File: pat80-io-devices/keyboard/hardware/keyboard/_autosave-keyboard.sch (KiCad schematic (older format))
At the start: 117 parts, among them J3 Keyboard connector, SW1 1, SW10 3, SW11 E, SW12 D, SW13 C, SW14 V, SW15 F, SW16 R, SW17 4, SW18 5, SW19 T, SW2 Q, SW20 G, SW21 B, SW22 N, SW23 H, SW24 Y, SW25 6, SW26 7, SW27 U, SW28 J, SW29 M, SW3 A, SW30 ', SW31 K, SW32 I, SW33 8, SW34 9, SW35 O, SW36 L, SW37 P, SW38 [, SW39 ], SW4 Z, SW40 0, SW41 BACKSPACE, SW42 TILDE, SW43 TAB, SW44 ,, SW45 ., SW46 SPACE, SW47 /, SW48 ;, SW49 LSHIFT, SW5 X, SW50 CTRL, SW51 RSHIFT, SW52 RETURN, SW53 PATO, SW54 CAPSLK, SW6 S, SW7 W, SW8 2, SW9 CAPSLK_LED

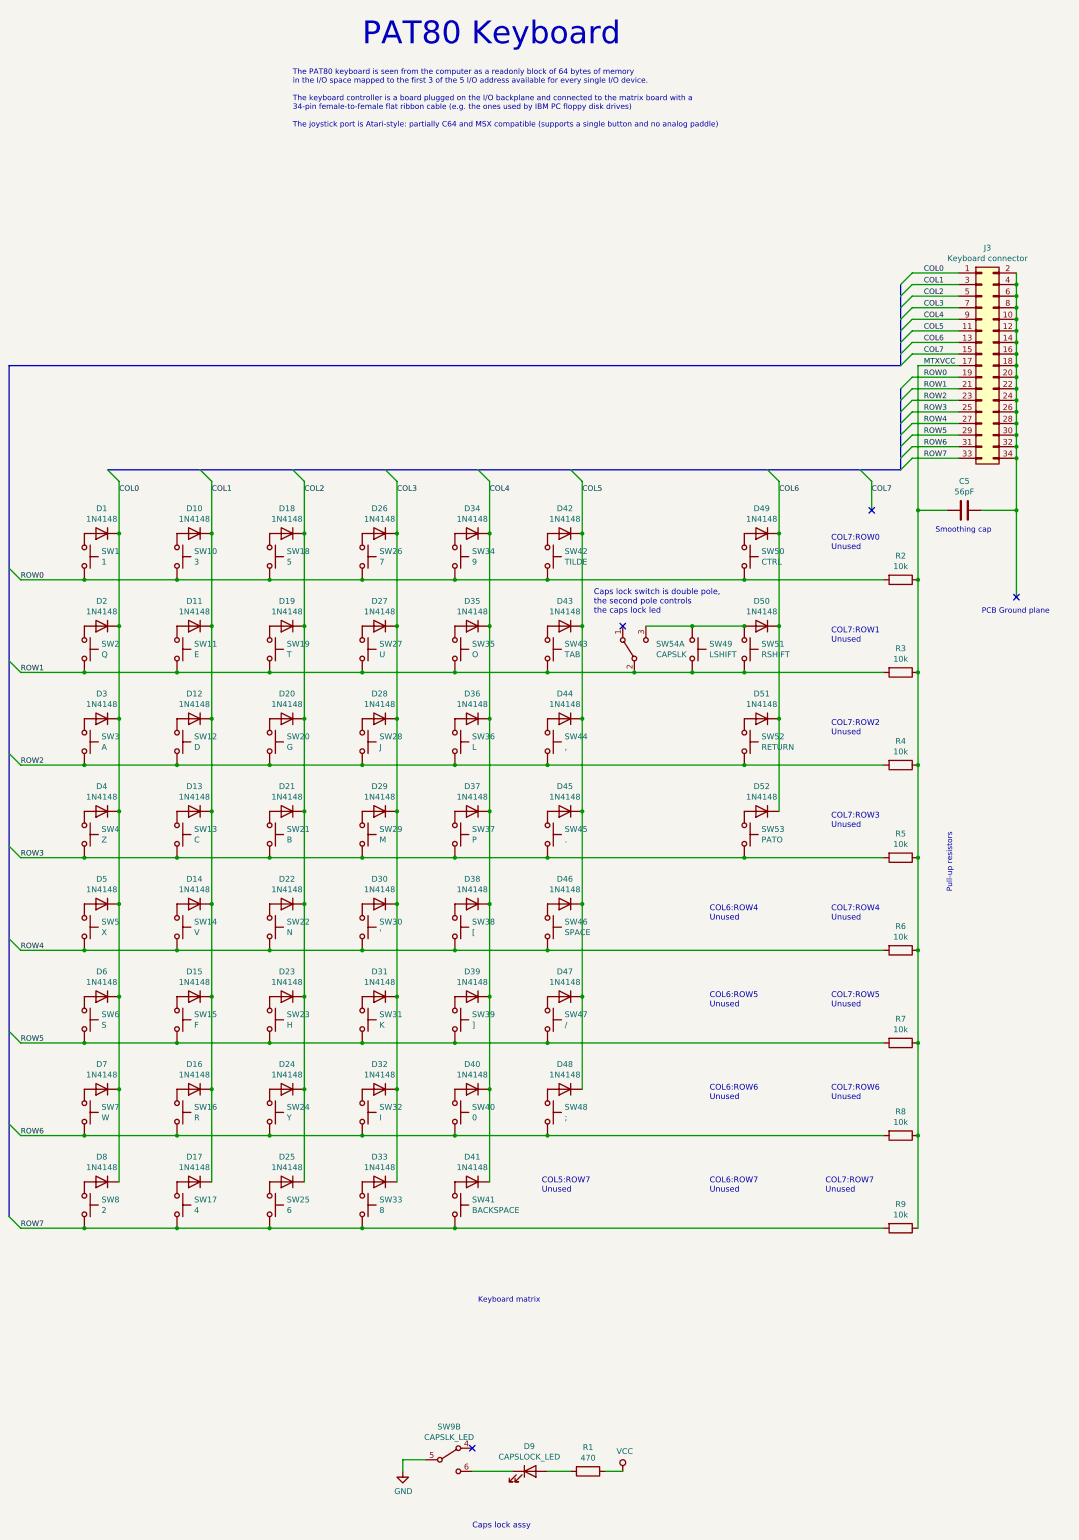
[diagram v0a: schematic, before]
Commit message: Split keyboard into two different schematics: kb controller and kb assembly. Started routing keyboard pcb.
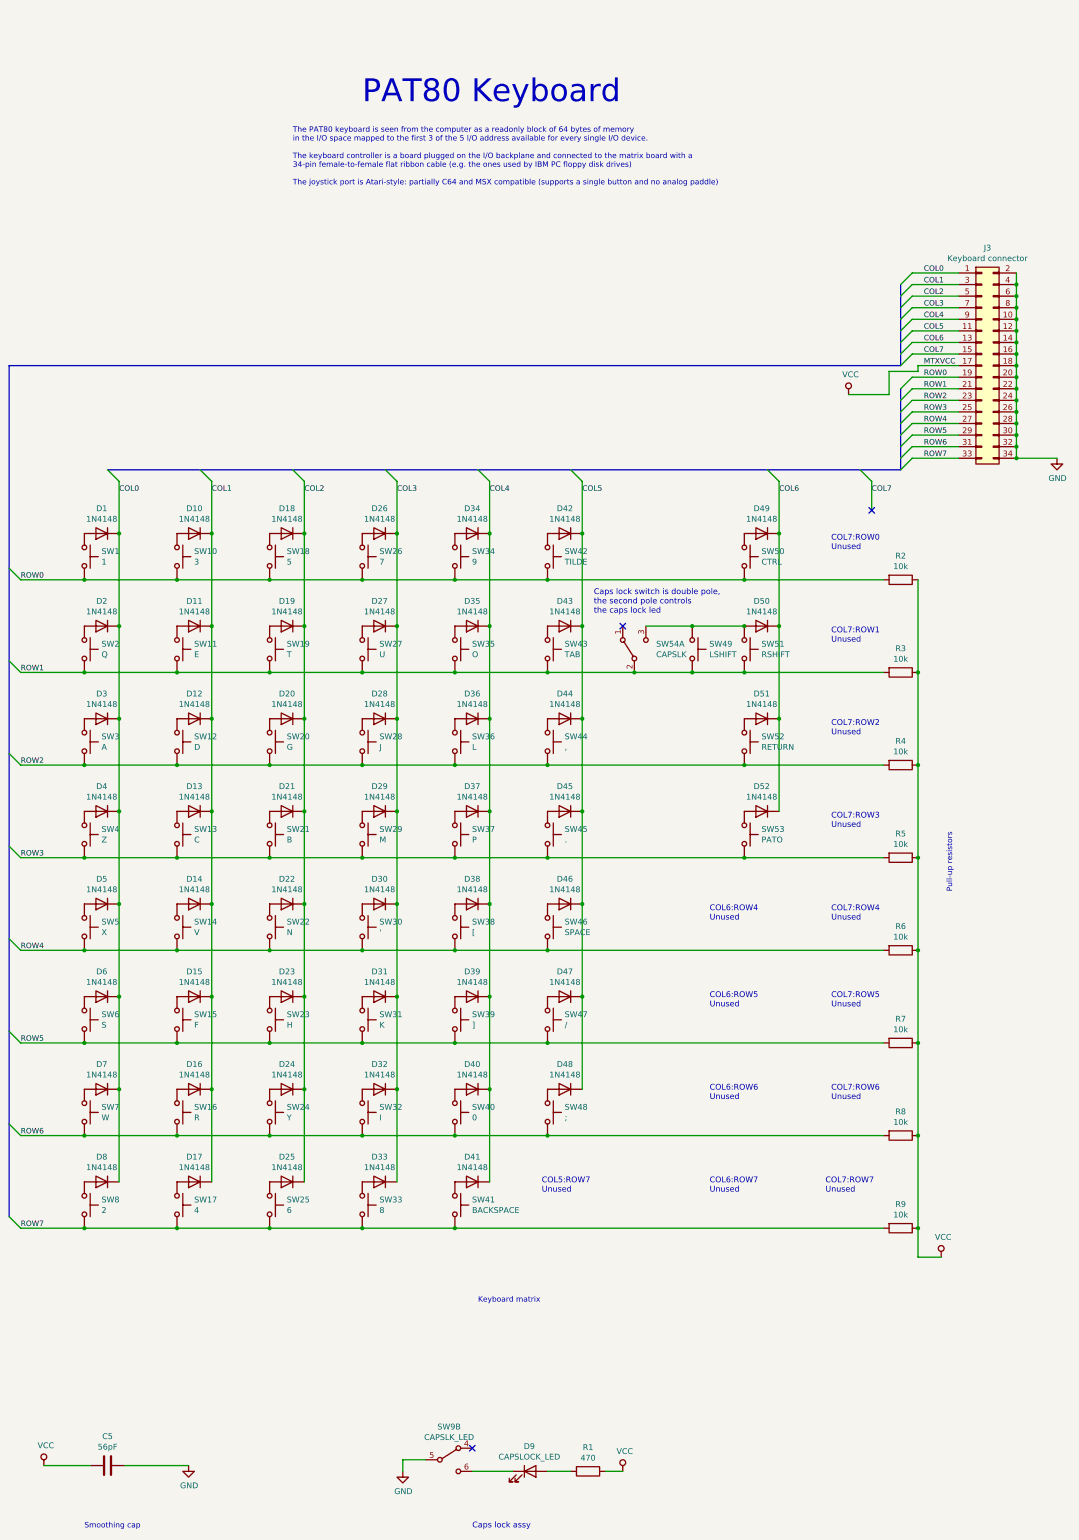
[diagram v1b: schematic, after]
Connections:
- net MTXVCC is gone; now on net VCC: C5.2, J3.17 (Pin_17), R2.1, R3.1, R4.1, R5.1, R6.1, R7.1, R8.1, R9.1
- net GND: now also C5.1, J3.10 (Pin_10), J3.12 (Pin_12), J3.14 (Pin_14), J3.16 (Pin_16), J3.18 (Pin_18), J3.2 (Pin_2), J3.20 (Pin_20), J3.22 (Pin_22), J3.24 (Pin_24), J3.26 (Pin_26), J3.28 (Pin_28), J3.30 (Pin_30), J3.32 (Pin_32), J3.34 (Pin_34), J3.4 (Pin_4), J3.6 (Pin_6), J3.8 (Pin_8)
- no-connect marks 4 -> 3
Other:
- note removed: "PCB Ground plane"
- moved on the sheet: C5
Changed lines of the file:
@@
 Comment4 ""
 $EndDescr
-Text Notes 4600 1050 0    197  ~ 0
+Text Notes 4600 1550 0    197  ~ 0
 PAT80 Keyboard
-Text Notes 4000 1750 0    47   ~ 0
+Text Notes 4000 2250 0    47   ~ 0
 The PAT80 keyboard is seen from the computer as a readonly block of 64 bytes of memory\nin the I/O space mapped to the first 3 of the 5 I/O address available for every single I/O device.\n\nThe keyboard controller is a board plugged on the I/O backplane and connected to the matrix board with a\n34-pin female-to-female flat ribbon cable (e.g. the ones used by IBM PC floppy disk drives)\n\nThe joystick port is Atari-style: partially C64 and MSX compatible (supports a single button and no analog paddle)
 $Comp
@@
 Text Label 9450 4600 0    47   ~ 0
 ROW7
-Connection ~ 10250 4600
 $Comp
 L Device:D D49
@@
 Wire Wire Line
 	9750 3800 9400 3800
-Wire Wire Line
-	9400 3800 9400 5050
 Text Label 9450 3800 0    47   ~ 0
 MTXVCC
@@
 L Device:C C5
 U 1 1 6159FE0F
-P 9800 5050
-F 0 "C5" V 9548 5050 50  0000 C CNN
-F 1 "56pF" V 9639 5050 50  0000 C CNN
-F 2 "Capacitor_THT:CP_Radial_Tantal_D6.0mm_P5.00mm" H 9838 4900 50  0001 C CNN
-F 3 "~" H 9800 5050 50  0001 C CNN
-	1    9800 5050
-	0    1    1    0
-$EndComp
-Wire Wire Line
-	9650 5050 9400 5050
-Connection ~ 9400 5050
-Wire Wire Line
-	9400 5050 9400 5650
-Text Notes 9550 5250 0    47   ~ 0
+P 2400 13300
+F 0 "C5" V 2148 13300 50  0000 C CNN
+F 1 "56pF" V 2239 13300 50  0000 C CNN
+F 2 "Capacitor_THT:CP_Radial_Tantal_D6.0mm_P5.00mm" H 2438 13150 50  0001 C CNN
+F 3 "~" H 2400 13300 50  0001 C CNN
+	1    2400 13300
+	0    1    1    0
+$EndComp
+Text Notes 2200 13850 0    47   ~ 0
 Smoothing cap\n
-NoConn ~ 10250 5800
-Text Notes 9950 5950 0    47   ~ 0
-PCB Ground plane
-Wire Wire Line
-	10250 4600 10250 5050
-Wire Wire Line
-	9950 5050 10250 5050
-Connection ~ 10250 5050
-Wire Wire Line
-	10250 5050 10250 5800
 Connection ~ 8200 5250
 Wire Wire Line
@@
 Text Notes 5600 11900 0    47   ~ 0
 Keyboard matrix
-Connection ~ 9400 5650
 Connection ~ 5700 6050
 Connection ~ 4900 6050
@@
 NoConn ~ 6850 6050
 NoConn ~ 5550 13150
+Wire Wire Line
+	9400 11250 9400 11500
+Wire Wire Line
+	9400 11500 9600 11500
+Connection ~ 9400 11250
+$Comp
+L power:VCC #PWR0101
+U 1 1 6076CE62
+P 9600 11500
+F 0 "#PWR0101" H 9600 11350 50  0001 C CNN
+F 1 "VCC" H 9617 11673 50  0000 C CNN
+F 2 "" H 9600 11500 50  0001 C CNN
+F 3 "" H 9600 11500 50  0001 C CNN
+	1    9600 11500
+	1    0    0    -1
+$EndComp
+Wire Wire Line
+	9400 3800 9400 3850
+$Comp
+L power:VCC #PWR0102
+U 1 1 6078C764
+P 8800 4050
+F 0 "#PWR0102" H 8800 3900 50  0001 C CNN
+F 1 "VCC" H 8817 4223 50  0000 C CNN
+F 2 "" H 8800 4050 50  0001 C CNN
+F 3 "" H 8800 4050 50  0001 C CNN
+	1    8800 4050
+	1    0    0    -1
+$EndComp
+Wire Wire Line
+	8800 4050 9150 4050
+Wire Wire Line
+	9150 4050 9150 3850
+Wire Wire Line
+	9150 3850 9400 3850
+Wire Wire Line
+	10250 4600 10600 4600
+Connection ~ 10250 4600
+$Comp
+L power:GND #PWR0103
+U 1 1 6079E0E1
+P 10600 4600
+F 0 "#PWR0103" H 10600 4350 50  0001 C CNN
+F 1 "GND" H 10605 4427 50  0000 C CNN
+F 2 "" H 10600 4600 50  0001 C CNN
+F 3 "" H 10600 4600 50  0001 C CNN
+	1    10600 4600
+	1    0    0    -1
+$EndComp
+$Comp
+L power:VCC #PWR0104
+U 1 1 607C8BE9
+P 1850 13300
+F 0 "#PWR0104" H 1850 13150 50  0001 C CNN
+F 1 "VCC" H 1867 13473 50  0000 C CNN
+F 2 "" H 1850 13300 50  0001 C CNN
+F 3 "" H 1850 13300 50  0001 C CNN
+	1    1850 13300
+	1    0    0    -1
+$EndComp
+Wire Wire Line
+	1850 13300 2250 13300
+$Comp
+L power:GND #PWR0105
+U 1 1 607D1F15
+P 3100 13300
+F 0 "#PWR0105" H 3100 13050 50  0001 C CNN
+F 1 "GND" H 3105 13127 50  0000 C CNN
+F 2 "" H 3100 13300 50  0001 C CNN
+F 3 "" H 3100 13300 50  0001 C CNN
+	1    3100 13300
+	1    0    0    -1
+$EndComp
+Wire Wire Line
+	3100 13300 2550 13300
 Wire Bus Line
 	9250 3100 9250 3800
